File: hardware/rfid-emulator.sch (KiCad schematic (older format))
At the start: 65 parts, among them J1 AVR-JTAG-10, J2 Conn_01x06, Q1 2N2907, Q2 5.8A/30V/35mΩ, Q3 ILL014NPbF, SW1 SW_Push, T1 2N2222, U1 ATmega64A-AU, U2 LM324, U3 LM317L_SO8, U4 TL431D, U5 LF50_TO252, U7 LF33_TO252, Y1 Crystal

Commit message: Update schematic with latest changes
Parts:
- removed C13, C17: 10n, symbol Device:C
- removed Q1: 2N2907, temp:TO18, symbol rfid-emulator-rescue:2N2907-temp-eagle-import
- removed Q2: 5.8A/30V/35mΩ, temp:SOT23-3, symbol rfid-emulator-rescue:MOSFET-NCH-AO3404A-temp-eagle-import
- removed R17: 56k, symbol Device:R
- removed R4, R5: (no value), temp:0603, symbol rfid-emulator-rescue:RESISTOR0603-temp-eagle-import
- removed T1: 2N2222, temp:TO18, symbol rfid-emulator-rescue:2N2222-temp-eagle-import
- added Q1: 2N3904, Package_TO_SOT_THT:TO-92_Inline, symbol Transistor_BJT:2N3904
- added Q2: 2N3906, Package_TO_SOT_THT:TO-92_Inline, symbol Transistor_BJT:2N3906
- added R5: 4.7k, symbol Device:R
- C10, C14: value 1n -> 0.1u
- C12, C16: value 10n -> 1.5n
- C9: value 1.5n -> 1.8n
- D2: value D -> 1N4148
- R11: value 2.2k -> 1k
- R12: value 56k -> 47k
- R15: value 1M -> 4.7k
- R16: value 2.2k -> 47k
- R6: value 100k -> 220k
- R7: value 1M -> 10
- gave numbers to parts that had none: 6
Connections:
- wire segments 195 -> 188
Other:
- moved on the sheet: C10, C12, C9, L1

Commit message: Update schematic to fix voltage supply, reflect prototyping changes
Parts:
- removed BT1: Battery, symbol Device:Battery
- removed C18: 2.2u, symbol Device:CP1
- removed Q3: ILL014NPbF, symbol Device:Q_NMOS_DGS
- removed R17: R_Variable, symbol Device:R_Variable
- removed U1: ATmega64A-AU, Package_QFP:TQFP-64_14x14mm_P0.8mm, symbol MCU_Microchip_ATmega:ATmega64A-AU
- removed U3: LM317L_SO8, Package_SO:SOIC-8_3.9x4.9mm_P1.27mm, symbol Regulator_Linear:LM317L_SO8
- removed U4: TL431D, Package_SO:SOIC-8_3.9x4.9mm_P1.27mm, symbol Reference_Voltage:TL431D
- removed U5: LF50_TO252, Package_TO_SOT_SMD:TO-252-2, symbol Regulator_Linear:LF50_TO252
- removed U6: LCD-016N002L, Display:LCD-016N002L, symbol Display_Character:LCD-016N002L
- added BT1: RJD3032, symbol Device:Battery_Cell
- added C17: 1n, symbol Device:C
- added C18, C21: 1u, symbol Device:C
- added C23: 0.1u, symbol Device:C_Small
- added C24: 10p, symbol Device:C_Small
- added C25, C31: 10n, symbol Device:C
- added C26, C27: 47p, symbol Device:C
- added C28, C30: 4.7u, symbol Device:C
- added C29: 100n, symbol Device:C
- added D5: Q_SCR_AGK, symbol Device:Q_SCR_AGK
- added D6: D, symbol Device:D
- added D7: LED_GREEN, symbol Device:LED
- added D8: D_TVS, symbol Device:D_TVS
- added FB2: Ferrite_Bead_Small, symbol Device:Ferrite_Bead_Small
- added J3: Conn_01x02_Male, symbol Connector:Conn_01x02_Male
- added JP1: CHARGE_SELECT, symbol Jumper:SolderJumper_3_Bridged12
- added JP2: ANT_SELECT, symbol Jumper:SolderJumper_3_Bridged12
- added L2: 3.9u, symbol Device:L
- added Q3, Q4: Q_PNP_BCE, symbol Device:Q_PNP_BCE
- added Q5, Q6: MOSFET-NCH-FQP30N06L, symbol rfid-emulator-eagle-import:MOSFET-NCH-FQP30N06L
- added R17, R20: 27, symbol Device:R
- added R19, R21, R24: 10k, symbol Device:R
- added R22: 22k, symbol Device:R
- added R23: 220, symbol Device:R
- added SW3, SW4: SW_Push, symbol Switch:SW_Push
- added SW_BACKLIGHT1: SW_SPST, symbol Switch:SW_SPST
- added TP1: VSUPPLY, symbol Connector:TestPoint
- added TP2: ANT, symbol Connector:TestPoint
- added TP3: DATA_IN_DIG, symbol Connector:TestPoint
- added TP4: DATA_IN_AN, symbol Connector:TestPoint
- added U1: NHD-C0216CiZ-FSW-FBW-3V3, symbol rfid-emulator:NHD-C0216CiZ-FSW-FBW-3V3
- added U3: LT8613, symbol rfid-emulator:LT8613
- added U4: ATmega64A-AU, Package_QFP:TQFP-64_14x14mm_P0.8mm, symbol MCU_Microchip_ATmega:ATmega64A-AU
- added U5: MCP73832-2-OT, Package_TO_SOT_SMD:SOT-23-5, symbol Battery_Management:MCP73832-2-OT
- added U6: FT230XS, Package_SO:SSOP-16_3.9x4.9mm_P0.635mm, symbol Interface_USB:FT230XS
- C12, C16: value 1.5n -> 470p
- C14, C15: value 0.1u -> 0.47u
- C20: value 10n -> 1n
- D4: Part (none) -> HSMQ-C170-T0000
- R10: value 1k -> 60.4k
- R11: value 1k -> 1k (GET RID OF THIS)
- R13: value 6k -> 1M
- R14: value 10k -> 243k
- R18: value 10k -> 8m
- R4: value 510 -> 220k
- R6: value 220k -> 560k
- R8, R9: value 0.47 -> 10k
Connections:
- net labels added: CHARGE_LT, CHARGE_MCP, DATA_IN_AN, DATA_IN_DIG, I2C_SCL, I2C_SDA, PRI_MID, UART0_RX, UART0_TX, VSUPPLY, ~I2C_RST~
- net labels removed: +2V5, DRIVER_EN, INT0, RFID_OUT, VBATT
- wire segments 188 -> 303
- no-connect marks 3 -> 1
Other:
- note added: "AVR MCU (David)"
- note added: "Antenna Driver (Noelle)"
- note added: "Antenna Load Switcher (Ian)"
- note added: "Antenna Signal Demodulator (David)"
- note added: "Charge Mode Select (David)"
- note added: "LCD (Noelle)"
- note added: "LT8613 Charging Circuit (Ian)"
- note added: "MCP73832 Charging Circuit (Optional) (David)"
- note added: "Micro USB Connection (Noelle)"
- note added: "USB-UART Module (Optional) (David)"
- note added: "Use a socket for this cap\nrather than SMT footprint"
- note added: "Voltage Regulator (Ian)"
- moved on the sheet: C1, C10, C11, C12, C13, C14, C16, C19, C2, C22, C3, C4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

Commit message: Add footprints for some components missing them
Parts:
- removed D6: D, symbol Device:D
- removed Q3, Q4: Q_PNP_BCE, symbol Device:Q_PNP_BCE
- removed SW2: Rotary_Encoder, symbol Device:Rotary_Encoder
- removed SW_BACKLIGHT1: SW_SPST, symbol Switch:SW_SPST
- added D6, D9: 1N4148, Diode_THT:D_DO-35_SOD27_P7.62mm_Horizontal, symbol Diode:1N4148
- added Q3: 2N3906, Package_TO_SOT_THT:TO-92_Inline, symbol Transistor_BJT:2N3906
- added SW2: EN11-HSM1BF20, rfid-footprints:EN11-HSM1BF20, symbol Device:Rotary_Encoder_Switch
- C1, C10, C11, C12, C13, C14, C16, C17, C2, C3, C4, C5, C6, C7, C8: footprint (none) -> Capacitors_SMD:C_0805_HandSoldering
- C15: footprint (none) -> Capacitors_SMD:C_0805_HandSoldering; Part (none) -> C0805C474K5RECTU
- C9: footprint (none) -> Socket_Strips:Socket_Strip_Straight_1x02_Pitch2.54mm
- J1: footprint (none) -> digikey-footprints:PinHeader_2x5_P2.54mm_Drill1.2mm; Part (none) -> 302-S101
- J2: value Conn_01x06 -> Micro_USB; footprint (none) -> Connectors_USB:USB_Micro-B_Molex_47346-0001; Part (none) -> Molex 47346-0001
- JP1, JP2: footprint (none) -> Jumper:SolderJumper-3_P1.3mm_Open_RoundedPad1.0x1.5mm
- TP1, TP2, TP3, TP4: footprint (none) -> Measurement_Points:Test_Point
- U1: footprint (none) -> rfid-footprints:NHD-C0216CiZ
- U3: footprint (none) -> Housings_DFN_QFN:QFN-28-1EP_3x6mm_Pitch0.5mm
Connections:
- net labels added: BKL_SW1, BKL_SW2
- wire segments 303 -> 307
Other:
- moved on the sheet: C15

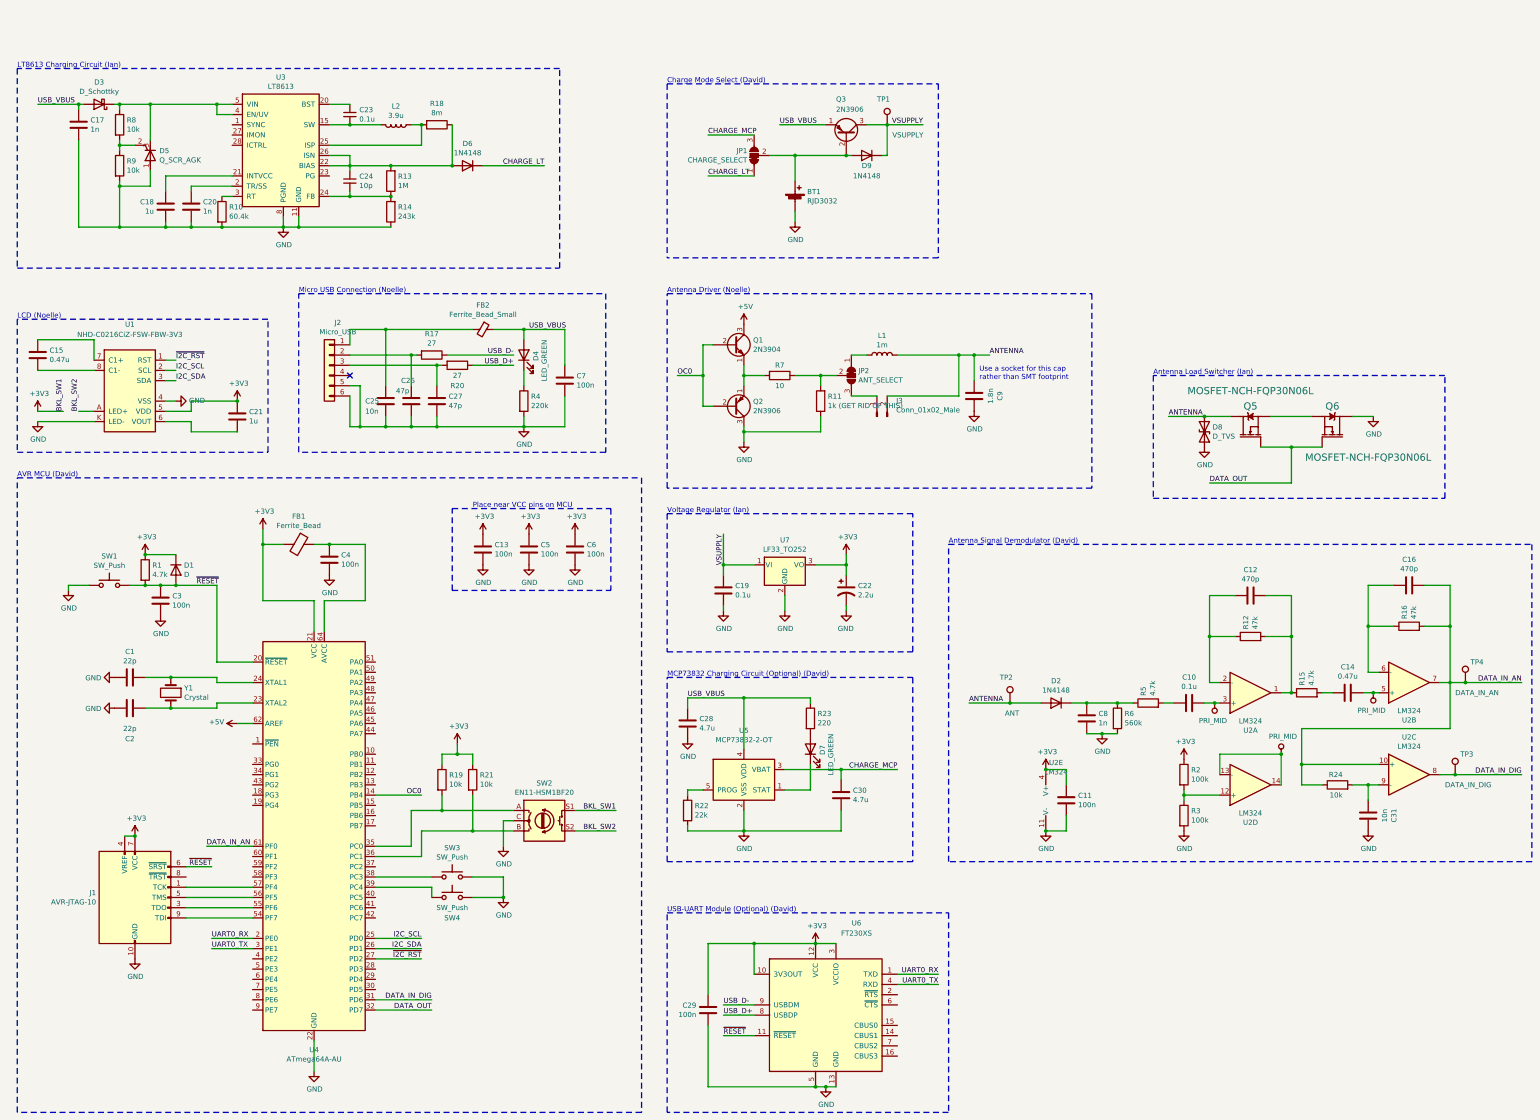
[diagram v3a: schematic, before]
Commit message: Add footprints for pretty much everything
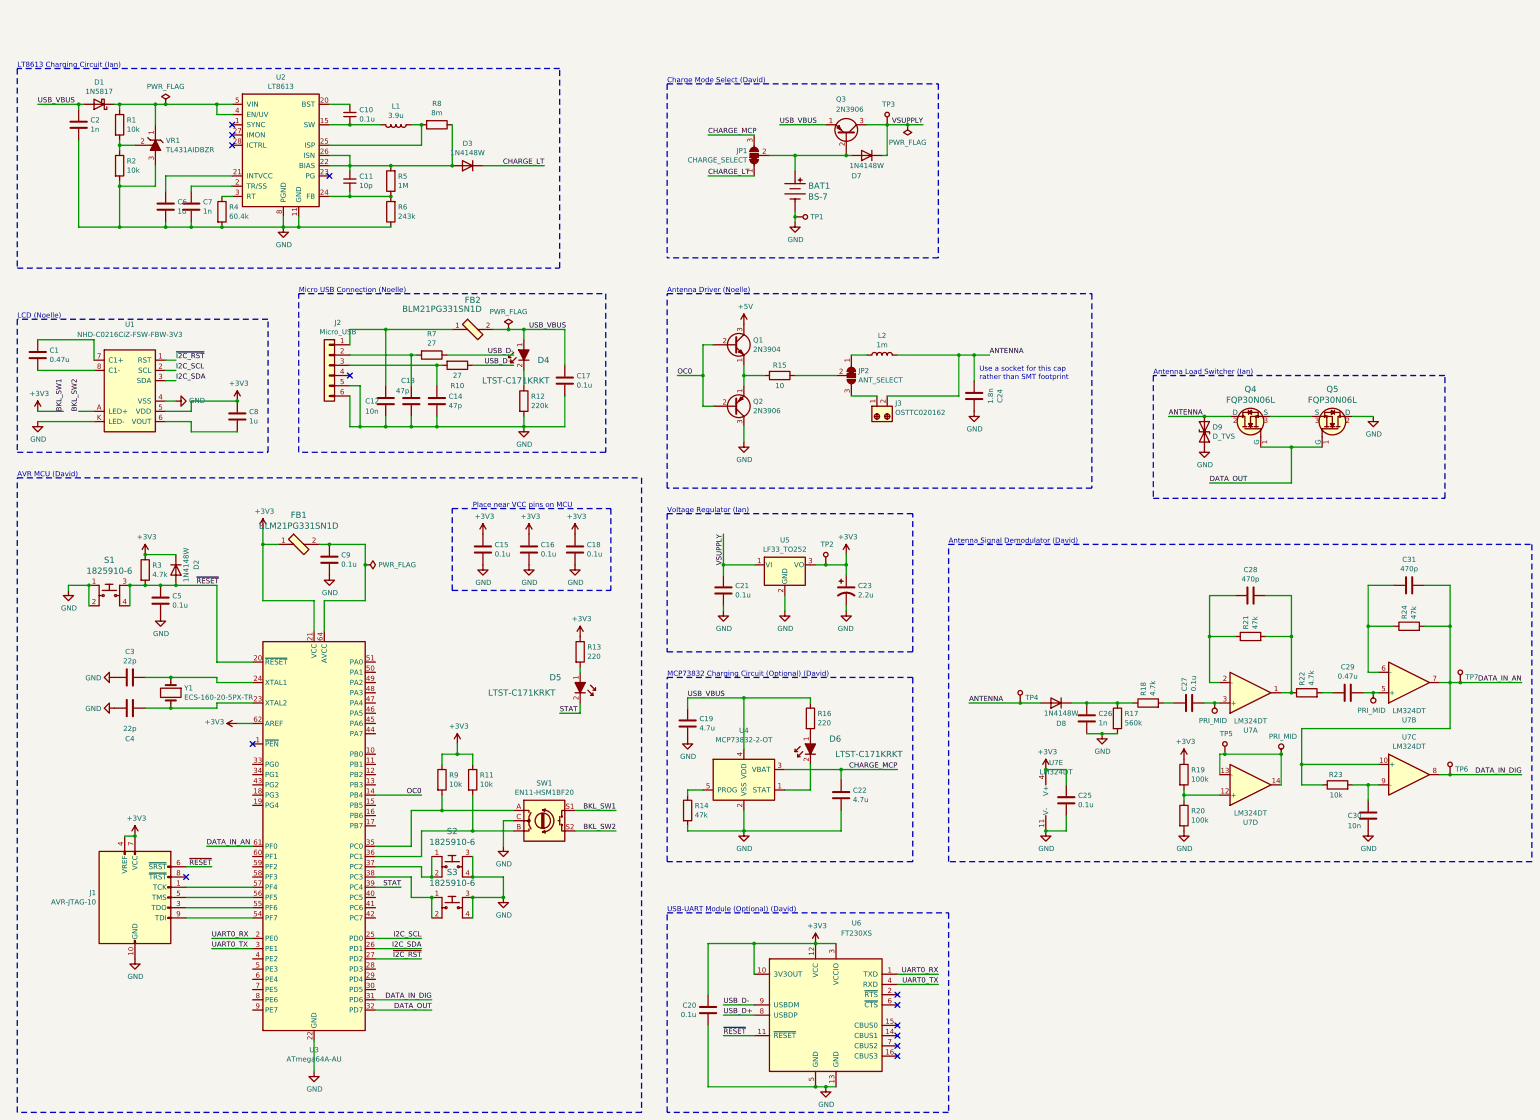
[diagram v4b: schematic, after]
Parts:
- removed BT1: RJD3032, symbol Device:Battery_Cell
- removed C10: 0.1u, Capacitors_SMD:C_0805_HandSoldering, symbol Device:C
- removed C11, C5: 100n, Capacitors_SMD:C_0805_HandSoldering, symbol Device:C
- removed C29: 100n, symbol Device:C
- removed C31: 10n, symbol Device:C
- removed D1: D, symbol Device:D
- removed D2: 1N4148, symbol Device:D
- removed D3: D_Schottky, symbol Device:D_Schottky
- removed D4, D7: LED_GREEN, symbol Device:LED
- removed D5: Q_SCR_AGK, symbol Device:Q_SCR_AGK
- removed D6, D9: 1N4148, Diode_THT:D_DO-35_SOD27_P7.62mm_Horizontal, symbol Diode:1N4148
- removed FB1: Ferrite_Bead, symbol Device:Ferrite_Bead
- removed FB2: Ferrite_Bead_Small, symbol Device:Ferrite_Bead_Small
- removed J3: Conn_01x02_Male, symbol Connector:Conn_01x02_Male
- removed Q5, Q6: MOSFET-NCH-FQP30N06L, symbol rfid-emulator-eagle-import:MOSFET-NCH-FQP30N06L
- removed R11: 1k (GET RID OF THIS), symbol Device:R
- removed SW1, SW3, SW4: SW_Push, symbol Switch:SW_Push
- removed TP1: VSUPPLY, Measurement_Points:Test_Point, symbol Connector:TestPoint
- removed TP2: ANT, Measurement_Points:Test_Point, symbol Connector:TestPoint
- removed TP3: DATA_IN_DIG, Measurement_Points:Test_Point, symbol Connector:TestPoint
- removed TP4: DATA_IN_AN, Measurement_Points:Test_Point, symbol Connector:TestPoint
- added BAT1: BS-7, digikey-footprints:Battery_Holder_Coin_2032_BS-7, symbol dk_Battery-Holders-Clips-Contacts:BS-7
- added C16, C17, C25, C27: 0.1u, Capacitors_SMD:C_0805_HandSoldering, symbol Device:C
- added C30: 10n, Capacitors_SMD:C_0805_HandSoldering, symbol Device:C
- added D1: 1N5817, Diodes_THT:D_DO-41_SOD81_P10.16mm_Horizontal, symbol Diode:1N5817
- added D2, D3, D7, D8: 1N4148W, Diodes_SMD:D_SOD-123, symbol Diode:1N4148W
- added D4, D5, D6: LTST-C171KRKT, digikey-footprints:0805, symbol dk_LED-Indication-Discrete:LTST-C171KRKT
- added FB1, FB2: BLM21PG331SN1D, digikey-footprints:0805, symbol dk_Ferrite-Beads-and-Chips:BLM21PG331SN1D
- added J3: OSTTC020162, digikey-footprints:Term_Block_1x2_P5mm, symbol dk_Terminal-Blocks-Wire-to-Board:OSTTC020162
- added Q4, Q5: FQP30N06L, digikey-footprints:TO-220-3, symbol dk_Transistors-FETs-MOSFETs-Single:FQP30N06L
- added R13: 220, Resistors_SMD:R_0805_HandSoldering, symbol Device:R
- added S1, S2, S3: 1825910-6, digikey-footprints:Switch_Tactile_THT_6x6mm, symbol dk_Tactile-Switches:1825910-6
- added TP1: 5001, digikey-footprints:Test_Point_D1.02mm, symbol dk_Test-Points:5001
- added TP2, TP3, TP5: 5000, digikey-footprints:Test_Point_D1.02mm, symbol dk_Test-Points:5000
- added TP4, TP6, TP7: 5002, digikey-footprints:Test_Point_D1.02mm, symbol dk_Test-Points:5002
- added VR1: TL431AIDBZR, digikey-footprints:SOT-23-3, symbol dk_PMIC-Voltage-Reference:TL431AIDBZR
- C10: renamed from C23; footprint (none) -> Capacitors_SMD:C_0805_HandSoldering; Part (none) -> C0805C104Z5VACTU
- C11: renamed from C24; footprint (none) -> Capacitors_SMD:C_0805_HandSoldering
- C12: renamed from C25; footprint (none) -> Capacitors_SMD:C_0805_HandSoldering; Part (none) -> C0805C103K1RAC7210
- C13: renamed from C26; footprint (none) -> Capacitors_SMD:C_0805_HandSoldering; Part (none) -> C0805C470J5GACTU
- C14: renamed from C27; footprint (none) -> Capacitors_SMD:C_0805_HandSoldering; Part (none) -> C0805C470J5GACTU
- C15: renamed from C13; value 100n -> 0.1u; Part (none) -> C0805C104Z5VACTU
- C18: value 1u -> 0.1u; footprint (none) -> Capacitors_SMD:C_0805_HandSoldering; Part (none) -> C0805C104Z5VACTU
- C19: renamed from C28; footprint (none) -> Capacitors_SMD:C_0805_HandSoldering; Part (none) -> CC0805ZRY5V6BB475
- C20: value 1n -> 0.1u; footprint (none) -> Capacitors_SMD:C_0805_HandSoldering; Part (none) -> C0805C104Z5VACTU
- C21: renamed from C19; footprint (none) -> Capacitors_SMD:C_0805_HandSoldering; Part (none) -> C0805C104Z5VACTU
- C22: renamed from C30; footprint (none) -> Capacitors_SMD:C_0805_HandSoldering; Part (none) -> CC0805ZRY5V6BB475
- C23: renamed from C22; footprint (none) -> rfid-footprints:EEE-1VA2R2NR; Part (none) -> EEE-1VA2R2NR
- C5: renamed from C3; value 100n -> 0.1u; Part (none) -> C0805C104Z5VACTU
- C6: value 100n -> 1u; Part (none) -> CC0805ZRY5V8BB105
- C7: value 100n -> 1n
- C8: renamed from C21; footprint (none) -> Capacitors_SMD:C_0805_HandSoldering; Part (none) -> CC0805ZRY5V8BB105
- C9: renamed from C4; value 100n -> 0.1u; Part (none) -> C0805C104Z5VACTU
- D9: renamed from D8; footprint (none) -> rfid-footprints:DO-219AD; Part (none) -> MSP3V3-M3/89A
- Q1, Q2, Q3: footprint Package_TO_SOT_THT:TO-92_Inline -> digikey-footprints:TO-92-3
- R1: renamed from R8; footprint (none) -> Resistors_SMD:R_0805_HandSoldering
- R10: renamed from R20; footprint (none) -> Resistors_SMD:R_0805_HandSoldering
- R11: renamed from R21; footprint (none) -> Resistors_SMD:R_0805_HandSoldering
- R12: renamed from R4; footprint (none) -> Resistors_SMD:R_0805_HandSoldering
- R14: renamed from R22; value 22k -> 47k; footprint (none) -> Resistors_SMD:R_0805_HandSoldering
- R15: renamed from R7; footprint (none) -> Resistors_SMD:R_0805_HandSoldering
- R16: renamed from R23; footprint (none) -> Resistors_SMD:R_0805_HandSoldering
- R17: renamed from R6; footprint (none) -> Resistors_SMD:R_0805_HandSoldering
- R18: renamed from R5; footprint (none) -> Resistors_SMD:R_0805_HandSoldering
- R19: renamed from R2; footprint (none) -> Resistors_SMD:R_0805_HandSoldering
- R2: renamed from R9; footprint (none) -> Resistors_SMD:R_0805_HandSoldering
- R20: renamed from R3; footprint (none) -> Resistors_SMD:R_0805_HandSoldering
- R21: renamed from R12; footprint (none) -> Resistors_SMD:R_0805_HandSoldering
- R22: renamed from R15; footprint (none) -> Resistors_SMD:R_0805_HandSoldering
- R23: renamed from R24; footprint (none) -> Resistors_SMD:R_0805_HandSoldering
- R24: renamed from R16; footprint (none) -> Resistors_SMD:R_0805_HandSoldering
- R3: renamed from R1; footprint (none) -> Resistors_SMD:R_0805_HandSoldering
- R4: renamed from R10; footprint (none) -> Resistors_SMD:R_0805_HandSoldering
- R5: renamed from R13; footprint (none) -> Resistors_SMD:R_0805_HandSoldering
- R6: renamed from R14; footprint (none) -> Resistors_SMD:R_0805_HandSoldering
- R7: renamed from R17; footprint (none) -> Resistors_SMD:R_0805_HandSoldering
- R8: renamed from R18; footprint (none) -> Resistors_SMD:R_0805_HandSoldering
- R9: renamed from R19; footprint (none) -> Resistors_SMD:R_0805_HandSoldering
- U3: renamed from U4; footprint Package_QFP:TQFP-64_14x14mm_P0.8mm -> Housings_QFP:TQFP-64_14x14mm_Pitch0.8mm
- U4: renamed from U5; footprint Package_TO_SOT_SMD:SOT-23-5 -> TO_SOT_Packages_SMD:SOT-23-5_HandSoldering
- U5: renamed from U7; footprint Package_TO_SOT_SMD:TO-252-2 -> TO_SOT_Packages_THT:TO-220-3_Horizontal
- U7: renamed from U2; value LM324 -> LM324DT; footprint (none) -> digikey-footprints:SOIC-14_W3.9mm
- Y1: value Crystal -> ECS-160-20-5PX-TR; footprint (none) -> rfid-footprints:XTAL_ECS-160-20-5PX-TR
- renumbered C15 to C1, C17 to C2, C9 to C24, C8 to C26, C12 to C28, C14 to C29, C1 to C3, C16 to C31, C2 to C4, L2 to L1, L1 to L2, SW2 to SW1, U3 to U2
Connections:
- net +3V3: now also C18.1, C20.1, U3.62 (AREF), C16.1, C25.1, D2.1 (K), FB1.1, R13.1, TP2.1; no longer C6.1
- net +5V: no longer U3.62 (AREF)
- net ANTENNA: now also D8.2 (A), J3.2, Q4.2 (D), TP4.1
- net CHARGE_LT: now also D3.1 (K)
- net DATA_IN_AN: now also TP7.1
- net DATA_IN_DIG: now also TP6.1
- net DATA_OUT: now also Q4.1 (G), Q5.1 (G)
- net GND: now also C18.2, C20.2, C7.1, BAT1.Neg, C16.2, C17.2, C25.2, C30.2, Q5.2 (D), S1.1, S1.2, S2.3, S2.4, S3.3, S3.4, TP1.1, VR1.3 (A); no longer C18.1, C20.1, C7.2
- net PRI_MID: now also C27.2, TP5.1
- net USB_VBUS: now also C17.1, D1.2 (A), D4.1, FB2.2; no longer C7.1
- net VSUPPLY: now also D7.1 (K), TP3.1
- net ~RESET~: now also D2.2 (A), S1.3, S1.4
- net at C9.1, U3.64 (AVCC): now also FB1.2
- net at C26.2, R17.1, R18.1: now also D8.1 (K)
- net at R18.2: now also C27.1
- net at JP1.2 (C), Q3.2 (B): now also BAT1.Pos, D7.2 (A)
- net at C12.1, J2.1 (Pin_1): now also FB2.1
- net at C11.1, R5.2, R8.1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: now also D3.2 (A)
- net at U3.37 (PC2): now also S2.1, S2.2
- net at U3.38 (PC3): now also S3.1, S3.2
- net STAT: now reaches U3.39 (PC4)
- net STAT: now also D5.2
- net at R23.2, U7.9 (-): now also C30.1
- net at R12.1: now also D4.2
- net at JP2.3 (B): now also J3.1
- net at U4.1 (STAT): now also D6.2
- net at R16.2: now also D6.1
- net at U2.2 (TR/SS): now also C7.2; no longer C20.2
- net at U2.21 (INTVCC): now also C6.1; no longer C18.2
- net at R1.1, U2.4 (EN/UV), U2.5 (VIN): now also D1.1 (K), VR1.1 (K)
- net at R1.2, R2.1: now also VR1.2 (REF)
- new net: Q4.3 (S), Q5.3 (S)
- new net: D5.1, R13.2
- no-connect marks 1 -> 13
